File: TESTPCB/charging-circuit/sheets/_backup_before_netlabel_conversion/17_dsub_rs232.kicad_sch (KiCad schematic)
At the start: 8 parts, among them P1 Header-Male-2.54_2x2, U8 MAX3232CDBR

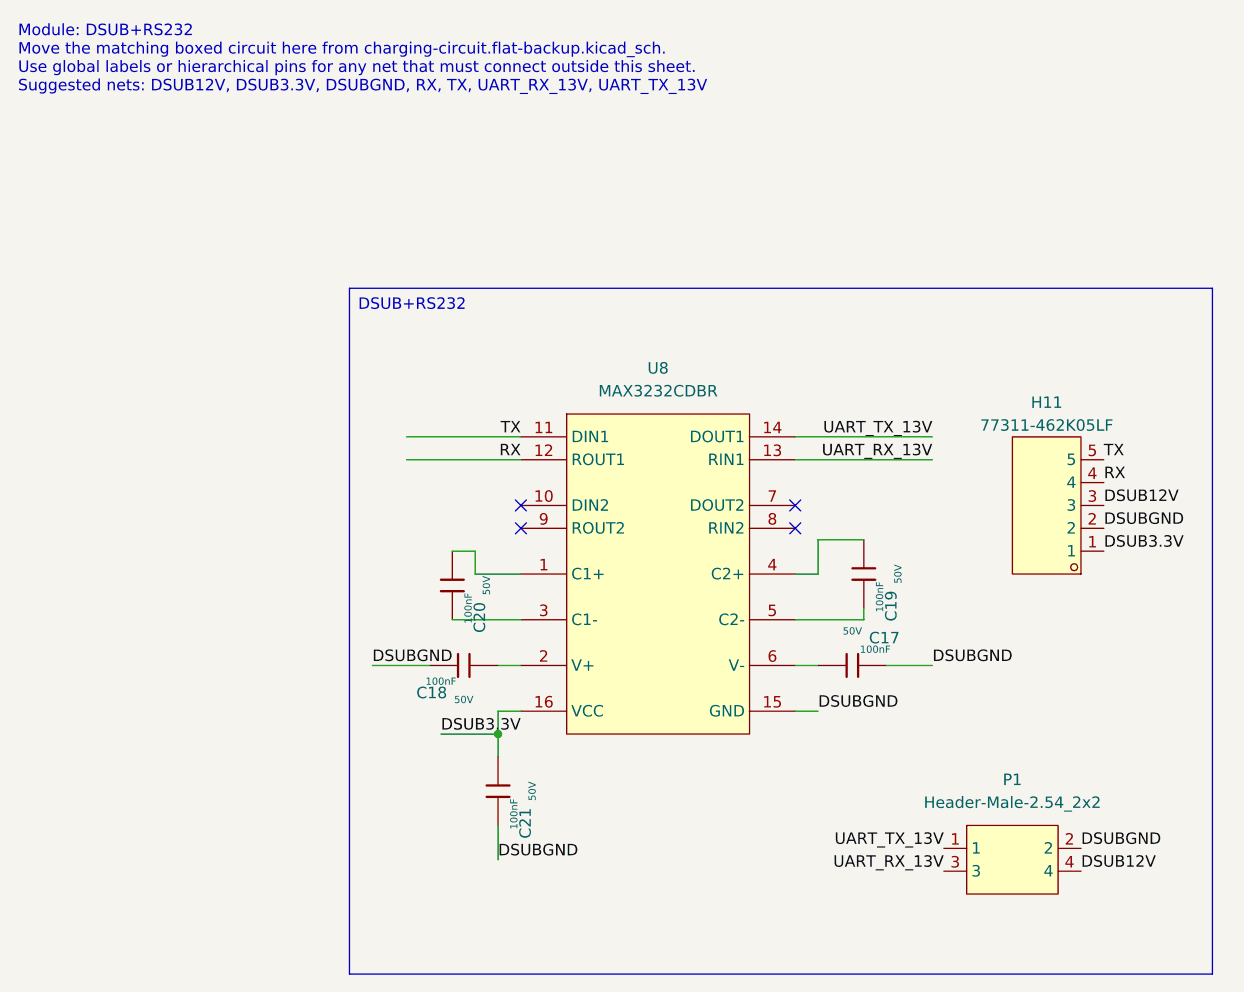
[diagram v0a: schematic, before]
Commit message: Fixed formatting issues, now the hierachal sheets are all labeled as net labels and when we want to expose their pins we will make them into hierchal or global pins
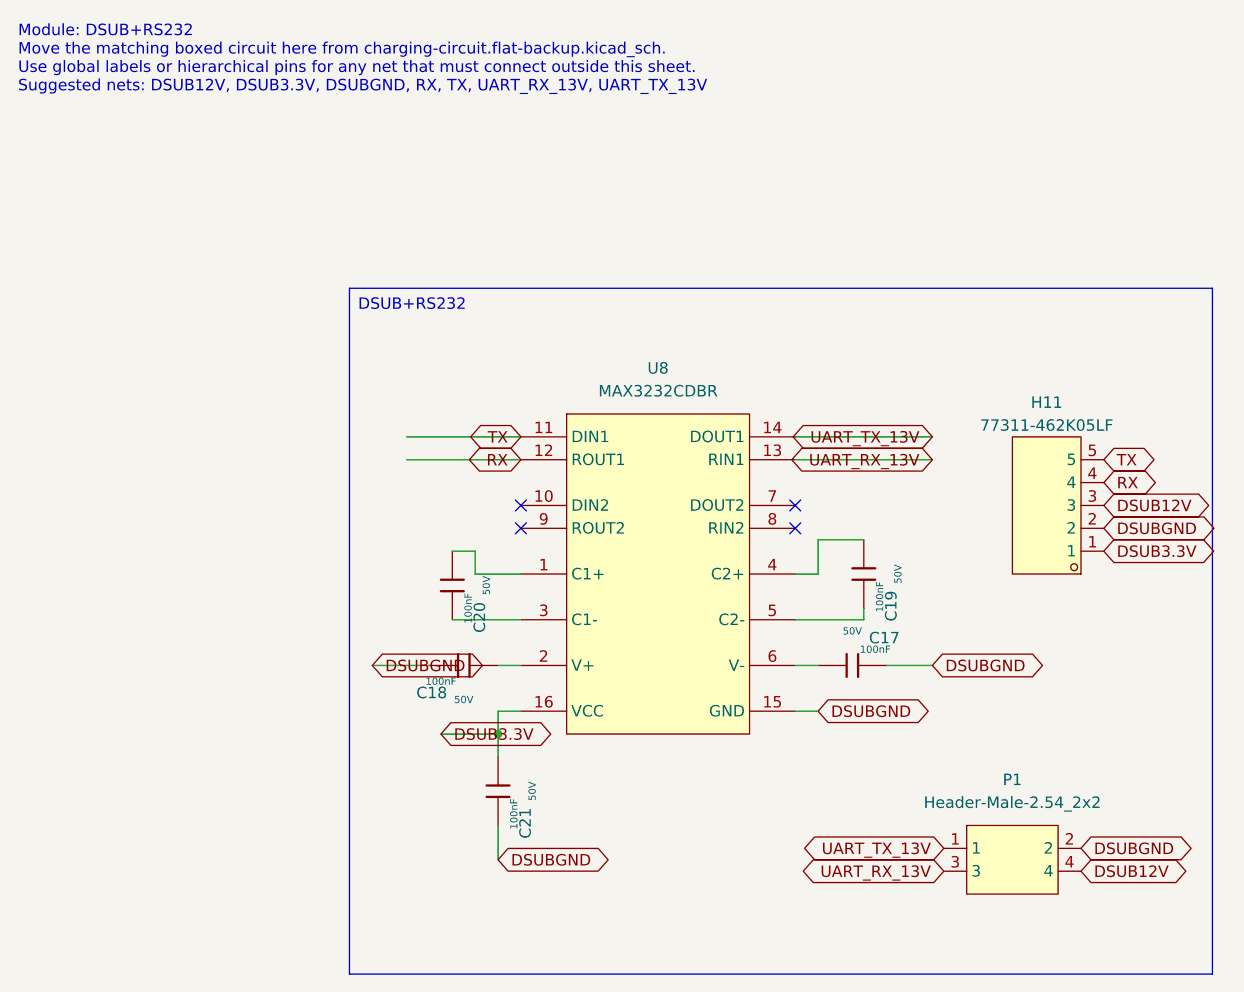
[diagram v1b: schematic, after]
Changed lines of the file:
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@@
 		)
 	)
-	(label "DSUBGND"
+	(global_label "DSUBGND"
+		(shape bidirectional)
 		(at 127 92.71 0)
 		(effects
@@
 			(justify left bottom)
 		)
-	)
-	(label "UART_RX_13V"
+		(property "Intersheetrefs" "${INTERSHEET_REFS}"
+			(at 127 92.71 0)
+			(effects
+				(font
+					(size 1.27 1.27)
+				)
+				(hide yes)
+			)
+		)
+	)
+	(global_label "UART_RX_13V"
+		(shape bidirectional)
 		(at 128.27 115.57 180)
 		(effects
@@
 			(justify right bottom)
 		)
-	)
-	(label "DSUBGND"
+		(property "Intersheetrefs" "${INTERSHEET_REFS}"
+			(at 128.27 115.57 0)
+			(effects
+				(font
+					(size 1.27 1.27)
+				)
+				(hide yes)
+			)
+		)
+	)
+	(global_label "DSUBGND"
+		(shape bidirectional)
 		(at 146.05 77.47 0)
 		(effects
@@
 			(justify left bottom)
 		)
-	)
-	(label "TX"
+		(property "Intersheetrefs" "${INTERSHEET_REFS}"
+			(at 146.05 77.47 0)
+			(effects
+				(font
+					(size 1.27 1.27)
+				)
+				(hide yes)
+			)
+		)
+	)
+	(global_label "TX"
+		(shape bidirectional)
 		(at 146.05 69.85 0)
 		(effects
@@
 			(justify left bottom)
 		)
-	)
-	(label "DSUBGND"
+		(property "Intersheetrefs" "${INTERSHEET_REFS}"
+			(at 146.05 69.85 0)
+			(effects
+				(font
+					(size 1.27 1.27)
+				)
+				(hide yes)
+			)
+		)
+	)
+	(global_label "DSUBGND"
+		(shape bidirectional)
 		(at 143.51 113.03 0)
 		(effects
@@
 			(justify left bottom)
 		)
-	)
-	(label "DSUB3.3V"
+		(property "Intersheetrefs" "${INTERSHEET_REFS}"
+			(at 143.51 113.03 0)
+			(effects
+				(font
+					(size 1.27 1.27)
+				)
+				(hide yes)
+			)
+		)
+	)
+	(global_label "DSUB3.3V"
+		(shape bidirectional)
 		(at 146.05 80.01 0)
 		(effects
@@
 			(justify left bottom)
 		)
-	)
-	(label "RX"
+		(property "Intersheetrefs" "${INTERSHEET_REFS}"
+			(at 146.05 80.01 0)
+			(effects
+				(font
+					(size 1.27 1.27)
+				)
+				(hide yes)
+			)
+		)
+	)
+	(global_label "RX"
+		(shape bidirectional)
 		(at 81.28 69.85 180)
 		(effects
@@
 			(justify right bottom)
 		)
-	)
-	(label "UART_TX_13V"
+		(property "Intersheetrefs" "${INTERSHEET_REFS}"
+			(at 81.28 69.85 0)
+			(effects
+				(font
+					(size 1.27 1.27)
+				)
+				(hide yes)
+			)
+		)
+	)
+	(global_label "UART_TX_13V"
+		(shape bidirectional)
 		(at 127 67.31 180)
 		(effects
@@
 			(justify right bottom)
 		)
-	)
-	(label "TX"
+		(property "Intersheetrefs" "${INTERSHEET_REFS}"
+			(at 127 67.31 0)
+			(effects
+				(font
+					(size 1.27 1.27)
+				)
+				(hide yes)
+			)
+		)
+	)
+	(global_label "TX"
+		(shape bidirectional)
 		(at 81.28 67.31 180)
 		(effects
@@
 			(justify right bottom)
 		)
-	)
-	(label "DSUBGND"
+		(property "Intersheetrefs" "${INTERSHEET_REFS}"
+			(at 81.28 67.31 0)
+			(effects
+				(font
+					(size 1.27 1.27)
+				)
+				(hide yes)
+			)
+		)
+	)
+	(global_label "DSUBGND"
+		(shape bidirectional)
 		(at 64.77 92.71 0)
 		(effects
@@
 			(justify left bottom)
 		)
-	)
-	(label "DSUB12V"
+		(property "Intersheetrefs" "${INTERSHEET_REFS}"
+			(at 64.77 92.71 0)
+			(effects
+				(font
+					(size 1.27 1.27)
+				)
+				(hide yes)
+			)
+		)
+	)
+	(global_label "DSUB12V"
+		(shape bidirectional)
 		(at 143.51 115.57 0)
 		(effects
@@
 			(justify left bottom)
 		)
-	)
-	(label "UART_TX_13V"
+		(property "Intersheetrefs" "${INTERSHEET_REFS}"
+			(at 143.51 115.57 0)
+			(effects
+				(font
+					(size 1.27 1.27)
+				)
+				(hide yes)
+			)
+		)
+	)
+	(global_label "UART_TX_13V"
+		(shape bidirectional)
 		(at 128.27 113.03 180)
 		(effects
@@
 			(justify right bottom)
 		)
-	)
-	(label "DSUBGND"
+		(property "Intersheetrefs" "${INTERSHEET_REFS}"
+			(at 128.27 113.03 0)
+			(effects
+				(font
+					(size 1.27 1.27)
+				)
+				(hide yes)
+			)
+		)
+	)
+	(global_label "DSUBGND"
+		(shape bidirectional)
 		(at 114.3 97.79 0)
 		(effects
@@
 			(justify left bottom)
 		)
-	)
-	(label "DSUB3.3V"
+		(property "Intersheetrefs" "${INTERSHEET_REFS}"
+			(at 114.3 97.79 0)
+			(effects
+				(font
+					(size 1.27 1.27)
+				)
+				(hide yes)
+			)
+		)
+	)
+	(global_label "DSUB3.3V"
+		(shape bidirectional)
 		(at 72.39 100.33 0)
 		(effects
@@
 			(justify left bottom)
 		)
-	)
-	(label "UART_RX_13V"
+		(property "Intersheetrefs" "${INTERSHEET_REFS}"
+			(at 72.39 100.33 0)
+			(effects
+				(font
+					(size 1.27 1.27)
+				)
+				(hide yes)
+			)
+		)
+	)
+	(global_label "UART_RX_13V"
+		(shape bidirectional)
 		(at 127 69.85 180)
 		(effects
@@
 			(justify right bottom)
 		)
-	)
-	(label "RX"
+		(property "Intersheetrefs" "${INTERSHEET_REFS}"
+			(at 127 69.85 0)
+			(effects
+				(font
+					(size 1.27 1.27)
+				)
+				(hide yes)
+			)
+		)
+	)
+	(global_label "RX"
+		(shape bidirectional)
 		(at 146.05 72.39 0)
 		(effects
@@
 			(justify left bottom)
 		)
-	)
-	(label "DSUBGND"
+		(property "Intersheetrefs" "${INTERSHEET_REFS}"
+			(at 146.05 72.39 0)
+			(effects
+				(font
+					(size 1.27 1.27)
+				)
+				(hide yes)
+			)
+		)
+	)
+	(global_label "DSUBGND"
+		(shape bidirectional)
 		(at 78.74 114.3 0)
 		(effects
@@
 			(justify left bottom)
 		)
-	)
-	(label "DSUB12V"
+		(property "Intersheetrefs" "${INTERSHEET_REFS}"
+			(at 78.74 114.3 0)
+			(effects
+				(font
+					(size 1.27 1.27)
+				)
+				(hide yes)
+			)
+		)
+	)
+	(global_label "DSUB12V"
+		(shape bidirectional)
 		(at 146.05 74.93 0)
 		(effects
@@
 			(justify left bottom)
 		)
-	)
+		(property "Intersheetrefs" "${INTERSHEET_REFS}"
+			(at 146.05 74.93 0)
+			(effects
+				(font
+					(size 1.27 1.27)
+				)
+				(hide yes)
+			)
+		)
+	)
